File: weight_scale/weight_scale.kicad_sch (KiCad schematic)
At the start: 8 parts, among them J1 Load cells, U1 MCP3421A0T-ECH, U2 ATmega169A-A

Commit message: add
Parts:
- added C10, C11: 10n, Capacitor_SMD:C_0805_2012Metric_Pad1.18x1.45mm_HandSolder, symbol Device:C
- added C2, C4, C6, C9: 100n, Capacitor_SMD:C_0805_2012Metric_Pad1.18x1.45mm_HandSolder, symbol Device:C
- added C3, C5: 10u, Capacitor_SMD:C_1206_3216Metric_Pad1.33x1.80mm_HandSolder, symbol Device:C_Polarized
- added C7, C8: DNP, Capacitor_SMD:C_0805_2012Metric_Pad1.18x1.45mm_HandSolder, symbol Device:C
- added D1: LED, LED_SMD:LED_0805_2012Metric_Pad1.15x1.40mm_HandSolder, symbol Device:LED
- added J2: ICSP_TagConnect, Connector:Tag-Connect_TC2030-IDC-NL_2x03_P1.27mm_Vertical, symbol Connector_Generic:Conn_01x06
- added J3: UART, Connector_PinSocket_2.54mm:PinSocket_1x05_P2.54mm_Vertical, symbol Connector_Generic:Conn_01x05
- added L1: 10u, symbol Device:L_Ferrite
- added R4: 1k, Resistor_SMD:R_0805_2012Metric_Pad1.20x1.40mm_HandSolder, symbol Device:R
- added SW1: USER, symbol Switch:SW_MEC_5E
- added Y1: DNP, Crystal:Crystal_C26-LF_D2.1mm_L6.5mm_Horizontal_1EP_style2, symbol Device:Crystal_GND3
- C1: footprint (none) -> Capacitor_SMD:C_0805_2012Metric_Pad1.18x1.45mm_HandSolder
- J1: footprint (none) -> Connector_Samtec_HPM_THT:Samtec_HPM-04-01-x-S_Straight_1x04_Pitch5.08mm
- NT1, R1, R2, R3: footprint (none) -> Resistor_SMD:R_0805_2012Metric_Pad1.20x1.40mm_HandSolder
- U1: footprint (none) -> Package_TO_SOT_SMD:SOT-23-6_Handsoldering
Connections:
- net +5V: now also C2.1, C4.1, C5.1, J2.1 (Pin_1), J3.3 (Pin_3)
- net GND: now also C2.2, C4.2, C5.2, C6.2, C7.2, C8.2, D1.1 (K), J2.3 (Pin_3), J3.1 (Pin_1), SW1.1, SW1.2, Y1.3
- net GNDA: now also C10.2, C11.1, C3.2
- net SCL: now also U2.6 (PE4)
- net SDA: now also U2.7 (PE5)
- net VDDA: now also C3.1
- net Vinn: now also J1.3 (Pin_3), C10.1, C9.2; no longer J1.2 (Pin_2)
- net Vinp: now also J1.2 (Pin_2), C11.2, C9.1; no longer J1.3 (Pin_3)
- net SCK: now reaches U2.11 (PB1)
- net SCK: now also J2.2 (Pin_2)
- net MOSI: now reaches U2.12 (PB2)
- net MOSI: now also J2.6 (Pin_6)
- net MISO: now reaches U2.13 (PB3)
- net MISO: now also J2.4 (Pin_4)
- net RX: now reaches U2.2 (PE0)
- net RX: now also J3.4 (Pin_4)
- net RST: now reaches U2.20 (PG5/~{RESET})
- net RST: now also J2.5 (Pin_5)
- net XT2: now reaches U2.23 (XTAL2)
- net XT2: now also C7.1, Y1.1
- net XT1: now reaches U2.24 (XTAL1)
- net XT1: now also C8.1, Y1.2
- net TX: now reaches U2.3 (PE1)
- net TX: now also J3.5 (Pin_5)
- net LED: now reaches U2.4 (PE2)
- net LED: now also R4.1
- net COM3: now reaches U2.48 (PA3)
- net COM2: now reaches U2.49 (PA2)
- net BTN: now reaches U2.5 (PE3)
- net BTN: now also C6.1, SW1.3 (K), SW1.4 (A)
- net COM1: now reaches U2.50 (PA1)
- net COM0: now reaches U2.51 (PA0)
- net at R3.2: now also L1.1
- new net: D1.2 (A), R4.2
- no-connect marks 0 -> 1
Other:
- company: (none) -> Xavier Bourlot
- title: (none) -> Load cell ctrl
- moved on the sheet: C1, NT1, R1, R2, R3, U1, U2

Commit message: a
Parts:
- removed D1: LED, LED_SMD:LED_0805_2012Metric_Pad1.15x1.40mm_HandSolder, symbol Device:LED
- added C12, C14: 10u, Capacitor_SMD:C_1206_3216Metric_Pad1.33x1.80mm_HandSolder, symbol Device:C_Polarized
- added C13, C16, C17, C18: 100n, Capacitor_SMD:C_0805_2012Metric_Pad1.18x1.45mm_HandSolder, symbol Device:C
- added C15: 1u, Capacitor_SMD:C_0805_2012Metric_Pad1.18x1.45mm_HandSolder, symbol Device:C
- added D1: LED_Dual, LED_SMD:LED_Cree-PLCC4_3.2x2.8mm_CCW, symbol Device:LED_Dual_AAKK
- added D2: CHG, LED_SMD:LED_0805_2012Metric_Pad1.15x1.40mm_HandSolder, symbol Device:LED
- added J4: BATT, Connector_PinHeader_2.54mm:PinHeader_1x02_P2.54mm_Horizontal, symbol Connector_Generic:Conn_01x02
- added J5: USB_B_Micro, Connector_USB:USB_Mini-B_Wuerth_65100516121_Horizontal, symbol Connector:USB_B_Micro
- added L2: 10u, Inductor_SMD:L_0805_2012Metric_Pad1.15x1.40mm_HandSolder, symbol Device:L_Ferrite
- added R5: 5k1, Resistor_SMD:R_0805_2012Metric_Pad1.20x1.40mm_HandSolder, symbol Device:R
- added R6, R9: 1k, Resistor_SMD:R_0805_2012Metric_Pad1.20x1.40mm_HandSolder, symbol Device:R
- added R7, R8: 100, Resistor_SMD:R_0805_2012Metric_Pad1.20x1.40mm_HandSolder, symbol Device:R
- added SW1: USER, symbol Switch:SW_MEC_5E
- added U3: MCP73831-2-OT, Package_TO_SOT_SMD:SOT-23-5, symbol Battery_Management:MCP73831-2-OT
- added U4: GDC0570, footprints:GDC0570_LCD_6digits_2mmPitch, symbol _MYLIBRARY:GDC0570_LCD_6digits
- L1: footprint (none) -> Inductor_SMD:L_0805_2012Metric_Pad1.15x1.40mm_HandSolder
- NT1: footprint Resistor_SMD:R_0805_2012Metric_Pad1.20x1.40mm_HandSolder -> NetTie:NetTie-2_SMD_Pad0.5mm
- R1, R2: value 5k6 -> 5k1
- renumbered SW1 to SW0
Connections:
- net +5V: now also C12.1, C13.1, J5.1 (VBUS), R6.1, U3.4 (V_{DD}); no longer C2.1, C4.1, C5.1, J2.1 (Pin_1), J3.3 (Pin_3), U2.21 (VCC), U2.52 (VCC), U2.64 (AVCC)
- net COM0: now also U4.17 (COM1)
- net COM1: now also U4.16 (COM2)
- net COM2: now also U4.15 (COM3)
- net COM3: now also U4.14 (COM4)
- net GND: now also C12.2, C13.2, C14.2, C15.2, C16.2, C17.2, C18.2, D1.3 (K1), D1.4 (K2), J4.2 (Pin_2), J5.5 (GND), J5.6 (Shield), R5.2, SW1.1, SW1.2, U3.2 (V_{SS})
- net GNDA: now also J1.4 (Pin_4); no longer J1.1 (Pin_1)
- net VDDA: now also L2.2; no longer J1.4 (Pin_4), R1.1, R2.1
- net Vinn: now also J1.2 (Pin_2), R8.1; no longer C10.1, C9.2, J1.3 (Pin_3), U1.6 (Vin-)
- net Vinp: now also J1.1 (Pin_1), R7.1; no longer C11.2, C9.1, J1.2 (Pin_2), U1.1 (Vin+)
- net Vlcdcap: now reaches U2.1 (LCDCAP)
- net Vlcdcap: now also C15.1
- net BTN0: now reaches U2.29 (PD4)
- net BTN0: now also C6.1, SW0.3 (K), SW0.4 (A)
- net BTN1: now reaches U2.30 (PD5)
- net BTN1: now also C17.1, SW1.3 (K), SW1.4 (A)
- net LED_0: now reaches U2.31 (PD6)
- net LED_0: now also R9.1
- net LED_1: now reaches U2.32 (PD7)
- net LED_1: now also R4.1
- net SEG12: now reaches U2.35 (PC0)
- net SEG12: now also U4.1
- net SEG11: now reaches U2.36 (PC1)
- net SEG11: now also U4.2
- net SEG10: now reaches U2.37 (PC2)
- net SEG10: now also U4.3
- net SEG9: now reaches U2.38 (PC3)
- net SEG9: now also U4.4
- net SEG8: now reaches U2.39 (PC4)
- net SEG8: now also U4.5
- net SEG7: now reaches U2.40 (PC5)
- net SEG7: now also U4.6
- net SEG6: now reaches U2.41 (PC6)
- net SEG6: now also U4.7
- net SEG5: now reaches U2.42 (PC7)
- net SEG5: now also U4.8
- net SEG4: now reaches U2.43 (PG2)
- net SEG4: now also U4.9
- net SEG3: now reaches U2.44 (PA7)
- net SEG3: now also U4.10
- net SEG2: now reaches U2.45 (PA6)
- net SEG2: now also U4.11
- net SEG1: now reaches U2.46 (PA5)
- net SEG1: now also U4.12
- net SEG0: now reaches U2.47 (PA4)
- net SEG0: now also U4.13
- net Aref: now reaches U2.62 (AREF)
- net Aref: now also C16.1
- net VDDF: now reaches U2.8 (PE6)
- net VDDF: now also R1.1, R2.1, C18.1
- net at R4.2: now also D1.1 (A1)
- net PWR_loadCell: now reaches L1.2
- net PWR_loadCell: now also U2.4 (PE2), U2.5 (PE3)
- removed net BTN: C6.1, SW0.3 (K), SW0.4 (A), U2.5 (PE3)
- removed net LED: R4.1, U2.4 (PE2)
- new net: D2.1 (K), U3.1 (STAT)
- new net: R5.1, U3.5 (PROG)
- new net: D2.2 (A), R6.2
- new net: D1.2 (A2), R9.2
- new net: J1.3 (Pin_3), L2.1
- new net +BATT: C14.1, C2.1, C4.1, C5.1, J2.1 (Pin_1), J3.3 (Pin_3), J4.1 (Pin_1), U2.21 (VCC), U2.52 (VCC), U2.64 (AVCC), U3.3 (V_{BAT})
- new net Vinn_f: C10.1, C9.2, R8.2, U1.6 (Vin-)
- new net Vinp_f: C11.2, C9.1, R7.2, U1.1 (Vin+)
- no-connect marks 1 -> 25
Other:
- note added: "1kV/10k=100mA"
- note added: "ON=Charging OFF=Complete"
- note added: "TODO: Check USB connector Check I2C pullup Check input filter Battery polarity"
- moved on the sheet: C1, C10, C11, C2, C3, C4, C5, C6, C7, C8, C9, J1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

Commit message: a
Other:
- note added: "TODO: Check USB connector Check I2C pullup Check input filter Battery polarity Button footprint"
- note removed: "TODO: Check USB connector Check I2C pullup Check input filter Battery polarity"
- moved on the sheet: C14, C2, C4, C5, J4

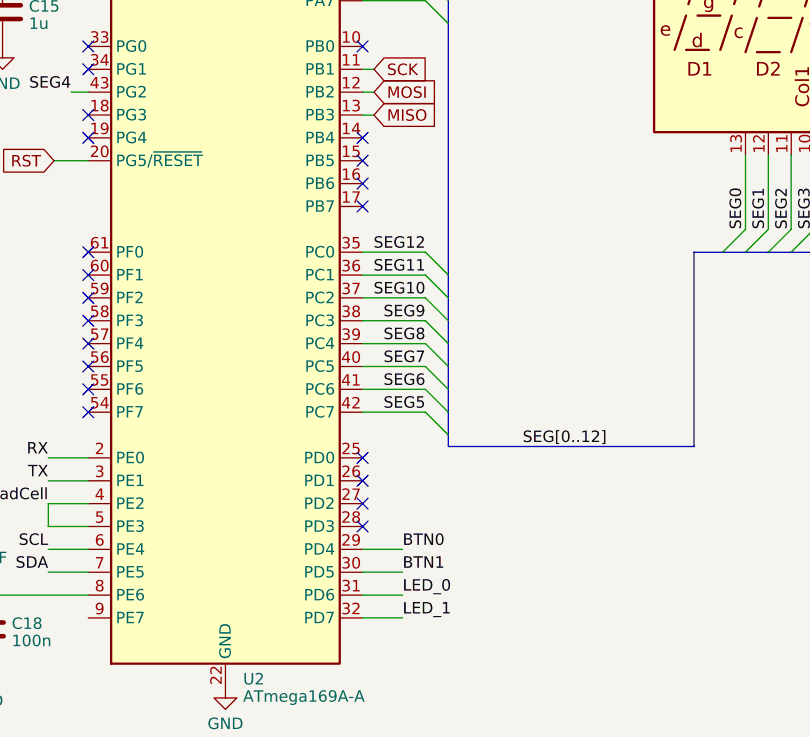
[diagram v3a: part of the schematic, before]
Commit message: PCINT and LCD low power
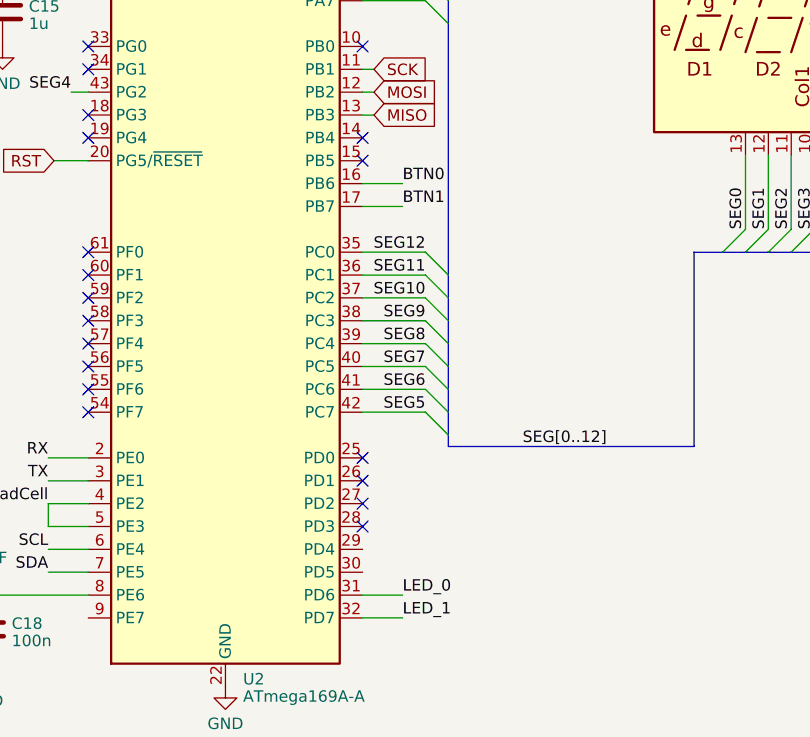
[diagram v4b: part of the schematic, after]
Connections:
- net BTN0: now also U2.16 (PB6); no longer U2.29 (PD4)
- net BTN1: now also U2.17 (PB7); no longer U2.30 (PD5)
- no-connect marks 25 -> 23
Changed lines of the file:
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@@
   (no_connect (at 75.565 146.685))
   (no_connect (at 106.045 169.545))
-  (no_connect (at 106.045 139.065))
   (no_connect (at 106.045 174.625))
   (no_connect (at 106.045 133.985))
@@
   (no_connect (at 24.13 104.14))
   (no_connect (at 75.565 123.825))
-  (no_connect (at 106.045 136.525))
   (bus_entry (at 113.03 98.425) (size 2.54 -2.54)
     (stroke (width 0) (type default))
@@
     (stroke (width 0) (type default))
   )
-  (wire (pts (xy 110.49 177.165) (xy 106.045 177.165))
+  (wire (pts (xy 110.49 136.525) (xy 106.045 136.525))
     (stroke (width 0) (type default))
   )
@@
     (stroke (width 0) (type default))
   )
-  (wire (pts (xy 110.49 179.705) (xy 106.045 179.705))
+  (wire (pts (xy 110.49 139.065) (xy 106.045 139.065))
     (stroke (width 0) (type default))
   )
@@
     (effects (font (size 1.27 1.27)) (justify right bottom))
   )
-  (label "BTN0" (at 110.49 177.165 0) (fields_autoplaced)
+  (label "BTN0" (at 110.49 136.525 0) (fields_autoplaced)
     (effects (font (size 1.27 1.27)) (justify left bottom))
   )
@@
     (effects (font (size 1.27 1.27)) (justify left bottom))
   )
-  (label "BTN1" (at 110.49 179.705 0) (fields_autoplaced)
+  (label "BTN1" (at 110.49 139.065 0) (fields_autoplaced)
     (effects (font (size 1.27 1.27)) (justify left bottom))
   )
